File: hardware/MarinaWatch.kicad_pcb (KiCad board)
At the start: 2 copper layers, 70 x 101 mm, 59 parts, among them J201 USB_C_Receptacle_USB2.0_16P, J401 Screw_Terminal_01x04, J801 Screw_Terminal_01x02, J802 Screw_Terminal_01x03, U101 ESP32-S3-MINI-1, U301 LMV321, U302 LMV321, U303 LMV321, U501 BQ24210, U601 BQ24210, U701 TPS63070

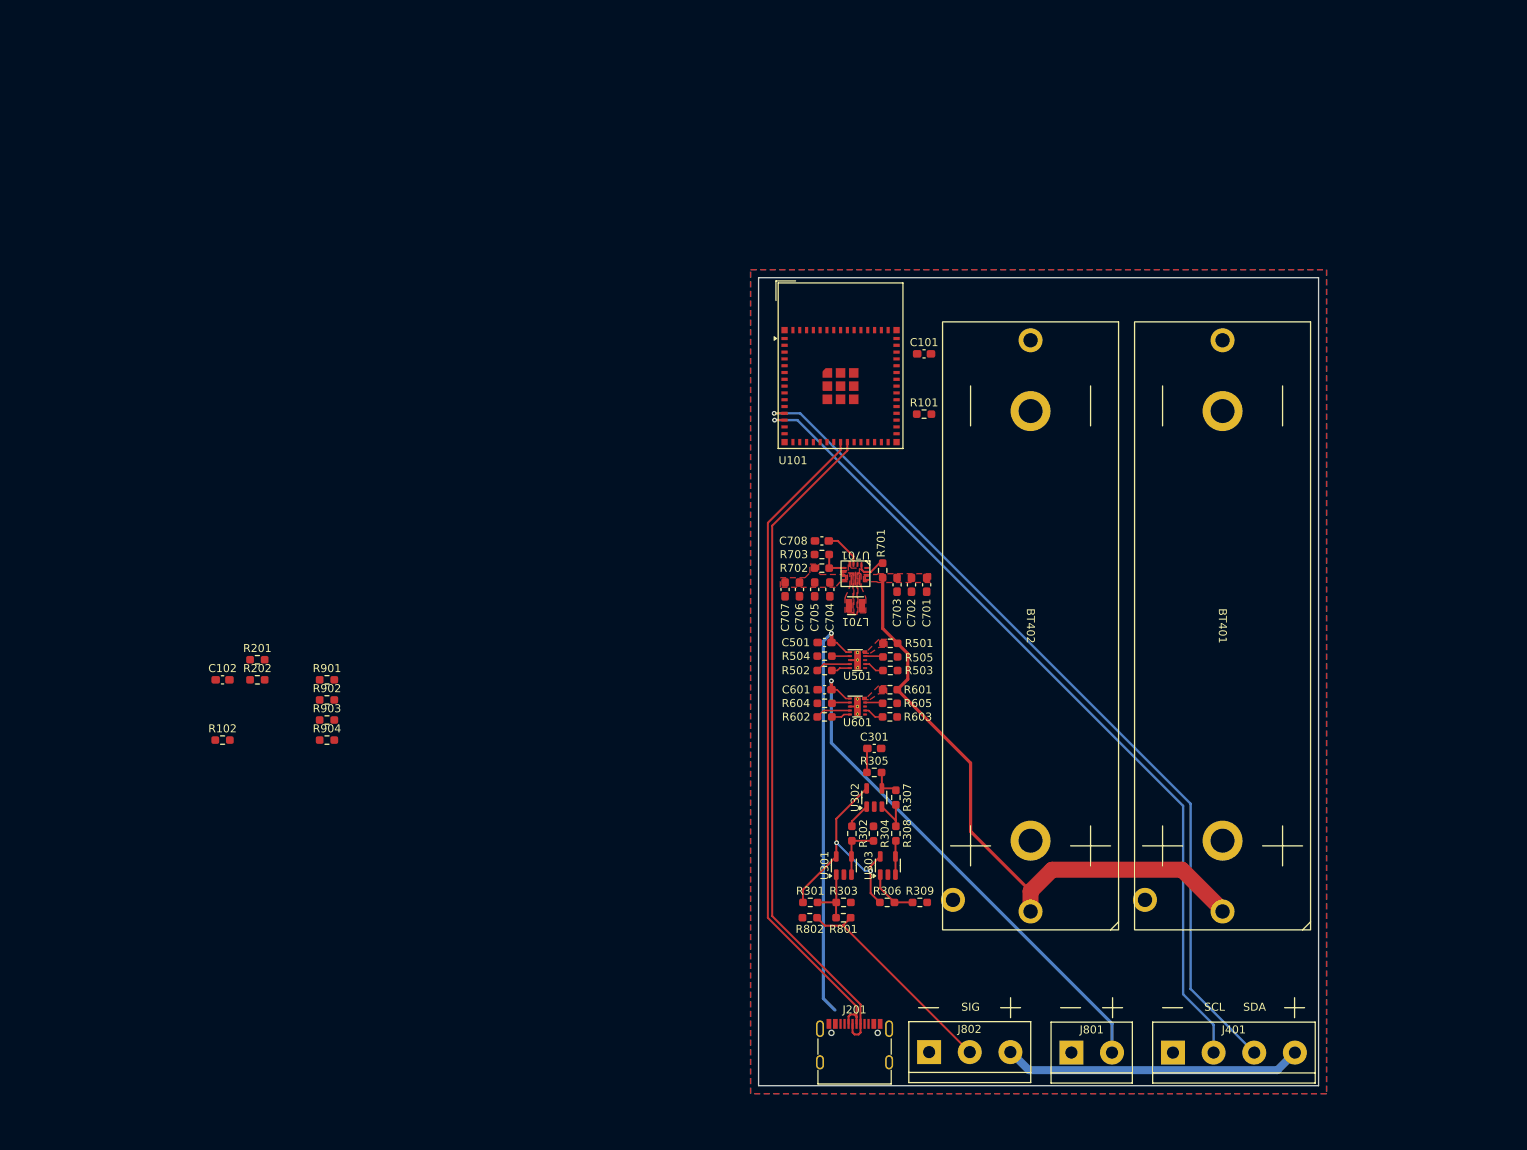
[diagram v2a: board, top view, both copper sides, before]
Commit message: Layout almost finished (missing NTCs and Buttons)
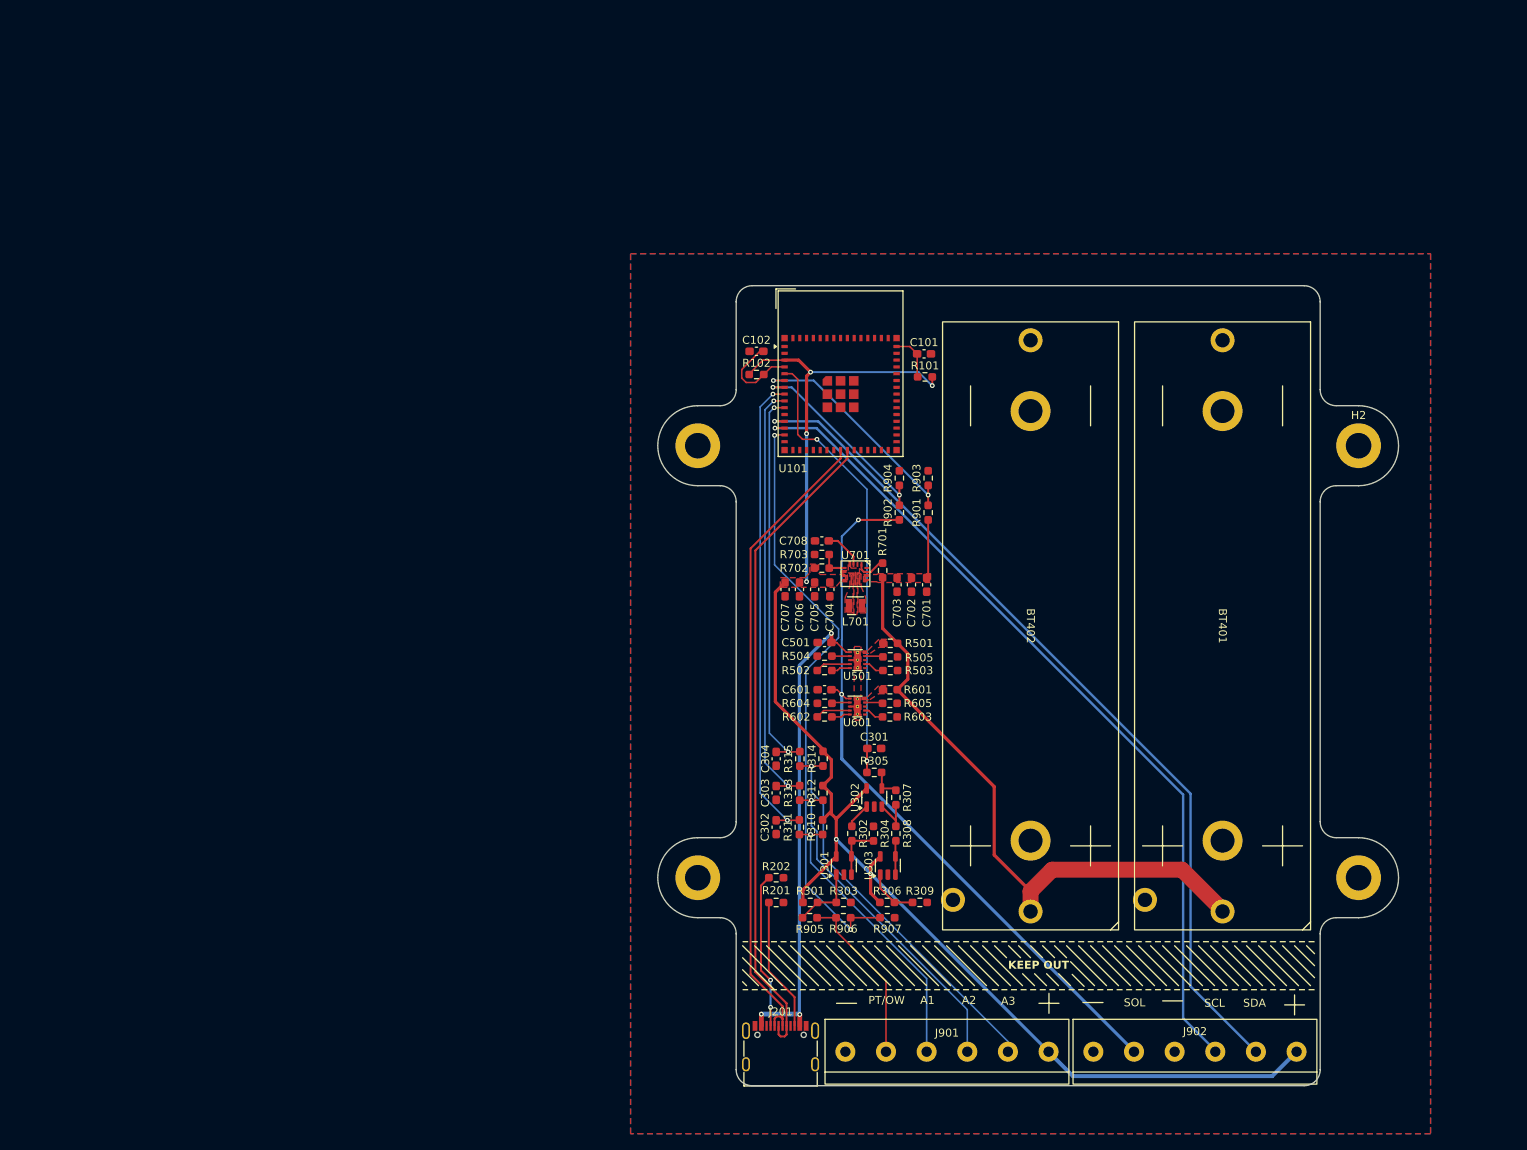
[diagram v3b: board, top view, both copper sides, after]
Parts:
- removed J401: Screw_Terminal_01x04, TerminalBlock:TerminalBlock_bornier-4_P5.08mm
- removed J801: Screw_Terminal_01x02, TerminalBlock:TerminalBlock_bornier-2_P5.08mm
- removed J802: Screw_Terminal_01x03, TerminalBlock:TerminalBlock_bornier-3_P5.08mm
- removed R801, R802: 100R, Resistor_SMD:R_0603_1608Metric_Pad0.98x0.95mm_HandSolder
- added C302: 22u, Capacitor_SMD:C_0603_1608Metric_Pad1.08x0.95mm_HandSolder, F.Cu at (128.2, 121.7)
- added C303: 22u, Capacitor_SMD:C_0603_1608Metric_Pad1.08x0.95mm_HandSolder, F.Cu at (128.2, 117.4)
- added C304: 22u, Capacitor_SMD:C_0603_1608Metric_Pad1.08x0.95mm_HandSolder, F.Cu at (128.2, 113.1)
- added H1: MountingHole_Pad, MountingHole:MountingHole_3.2mm_M3_DIN965_Pad, F.Cu at (118.4, 74.0)
- added H2: MountingHole_Pad, MountingHole:MountingHole_3.2mm_M3_DIN965_Pad, F.Cu at (201.0, 74.0)
- added H3: MountingHole_Pad, MountingHole:MountingHole_3.2mm_M3_DIN965_Pad, F.Cu at (118.4, 128.0)
- added H4: MountingHole_Pad, MountingHole:MountingHole_3.2mm_M3_DIN965_Pad, F.Cu at (201.0, 128.0)
- added J901: Screw_Terminal_01x06, AlfredLib:THT_SCREW_01x06_P5.08mm, F.Cu at (149.6, 149.8)
- added J902: Screw_Terminal_01x06, AlfredLib:THT_SCREW_01x06_P5.08mm, F.Cu at (180.6, 149.8)
- added R310: 10k, Resistor_SMD:R_0603_1608Metric_Pad0.98x0.95mm_HandSolder, F.Cu at (134.0, 121.7)
- added R311: 100R, Resistor_SMD:R_0603_1608Metric_Pad0.98x0.95mm_HandSolder, F.Cu at (131.1, 121.7)
- added R312: 10k, Resistor_SMD:R_0603_1608Metric_Pad0.98x0.95mm_HandSolder, F.Cu at (134.0, 117.4)
- added R313: 100R, Resistor_SMD:R_0603_1608Metric_Pad0.98x0.95mm_HandSolder, F.Cu at (131.1, 117.4)
- added R314: 10k, Resistor_SMD:R_0603_1608Metric_Pad0.98x0.95mm_HandSolder, F.Cu at (134.1, 113.1)
- added R315: 100R, Resistor_SMD:R_0603_1608Metric_Pad0.98x0.95mm_HandSolder, F.Cu at (131.2, 113.1)
- added R905: 0R, Resistor_SMD:R_0603_1608Metric_Pad0.98x0.95mm_HandSolder, F.Cu at (132.4, 133.0)
- added R906: 0R, Resistor_SMD:R_0603_1608Metric_Pad0.98x0.95mm_HandSolder, F.Cu at (136.6, 133.0)
- added R907: 10k, Resistor_SMD:R_0603_1608Metric_Pad0.98x0.95mm_HandSolder, F.Cu at (142.1, 133.0)
- moved R903 81.0 mm to (147.2, 78.0), turned to 90 degrees
- moved R102 80.9 mm to (125.7, 65.1)
- moved R904 78.7 mm to (143.6, 78.0), turned to 90 degrees
- moved C102 78.4 mm to (125.7, 62.2), turned to 180 degrees
- moved R901 78.0 mm to (147.2, 82.4), turned to 90 degrees
- moved R902 75.3 mm to (143.6, 82.4), turned to 90 degrees
- moved R201 71.6 mm to (128.2, 131.1)
- moved R202 69.4 mm to (128.2, 128.0)
- moved J201 9.25 mm to (128.8, 150.2)
- moved R101 4.65 mm to (146.8, 65.4), turned to 180 degrees
- moved U101 1.00 mm to (136.2, 65.0)
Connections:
- net Net-(J201-CC1) renamed /CC1
- net Net-(J201-CC2) renamed /CC2
- U101 pad 10: unconnected-(U101-IO6-Pad10) -> /A3
- U101 pad 8: unconnected-(U101-IO4-Pad8) -> /A1
- U101 pad 9: unconnected-(U101-IO5-Pad9) -> /A2
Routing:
- net +3V3: track 67.4 -> 183.5 mm, vias 2 -> 6
- net /ONE_WIRE: track 0.00 -> 75.6 mm, vias 0 -> 2
- net /A1: track 0.00 -> 59.7 mm, vias 0 -> 2
- net /TEMP_SENS: track 3.02 -> 57.3 mm, vias 0 -> 2
- net /A2: track 0.00 -> 54.1 mm, vias 0 -> 2
- net /ANALOG_3: track 0.00 -> 48.8 mm, vias 0 -> 1
- net /A3: track 0.00 -> 48.5 mm, vias 0 -> 2
- net /ANALOG_2: track 0.00 -> 42.4 mm, vias 0 -> 1
- net /ANALOG_1: track 0.00 -> 36.1 mm, vias 0 -> 1
- net /BAT_SENSE: track 0.00 -> 29.2 mm, vias 0 -> 2
- net SOLAR: track 64.9 -> 90.4 mm, vias 1 -> 2
- net /SOLAR_SENSE: track 0.00 -> 25.4 mm, vias 0 -> 2
- net /CC1: track 0.00 -> 19.4 mm, vias 0 -> 2
- net /CC2: track 0.00 -> 16.8 mm
- net /BOOT: track 0.00 -> 11.2 mm
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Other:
- board size 70 x 101 mm -> 92.6 x 100 mm
- board text added: "A1"
- board text added: "A2"
- board text added: "A3"
- board text added: "KEEP OUT"
- board text added: "PT/OW"
- board text added: "SOL"
- board text removed: "SIG"

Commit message: First draft of HW and moved scripts
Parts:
- added C103: 10u, Capacitor_SMD:C_0603_1608Metric_Pad1.08x0.95mm_HandSolder, F.Cu at (117.5, 99.4)
- added SW101: SW_Push, AlfredLib:BUTTON_SMD_3x4mm, F.Cu at (130.5, 32.7)
- added SW102: SW_Push, AlfredLib:BUTTON_SMD_3x4mm, F.Cu at (117.3, 110.9)
- added U304: ESP32-S3-WROOM-1, RF_Module:ESP32-S3-WROOM-1, F.Cu at (134.2, 67.1)
- R101, R102, R503, R603, R701: value 5k1 -> 10k
- R504: value 5k1 -> 511R
- R505: value 5k1 -> 6k8
- R605: value 5k1 -> 0R
- R904: value 7k5 -> 3k
- moved U101 115.0 mm to (41.5, 130.3)
- moved C101 42.8 mm to (130.9, 22.8)
- moved R101 42.8 mm to (131.1, 25.6)
- moved C102 41.5 mm to (116.3, 102.6), turned to 90 degrees
- moved R102 38.3 mm to (118.0, 102.6), turned to -90 degrees
- moved R902 5.23 mm to (144.5, 87.5)
- moved R904 5.23 mm to (144.5, 83.2)
- moved R901 5.05 mm to (147.4, 87.4)
- moved R903 5.05 mm to (147.4, 83.1)
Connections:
- U101 pad 10: /A3 -> unconnected-(U101-IO6-Pad10)
- U101 pad 12: /I2C_SDA -> unconnected-(U101-IO8-Pad12)
- U101 pad 13: /I2C_SCL -> unconnected-(U101-IO9-Pad13)
- U101 pad 14: /ONE_WIRE -> unconnected-(U101-IO10-Pad14)
- U101 pad 23: /D- -> unconnected-(U101-IO19-Pad23)
- U101 pad 24: /D+ -> unconnected-(U101-IO20-Pad24)
- U101 pad 4: /BOOT -> unconnected-(U101-IO0-Pad4)
- U101 pad 45: /RESET -> unconnected-(U101-EN-Pad45)
- U101 pad 5: /TEMP_SENS -> unconnected-(U101-IO1-Pad5)
- U101 pad 6: /BAT_SENSE -> unconnected-(U101-IO2-Pad6)
- U101 pad 7: /SOLAR_SENSE -> unconnected-(U101-IO3-Pad7)
- U101 pad 8: /A1 -> unconnected-(U101-IO4-Pad8)
- U101 pad 9: /A2 -> unconnected-(U101-IO5-Pad9)
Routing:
- net /I2C_SDA: track 108.2 -> 35.6 mm, vias 1 -> 0
- net /I2C_SCL: track 105.0 -> 33.8 mm, vias 1 -> 0
- net +3V3: track 183.5 -> 154.9 mm, vias 6 -> 4
- net /SOLAR_SENSE: track 25.4 -> 2.49 mm, vias 2 -> 0
- net /D+: track 81.7 -> 73.8 mm
- net +BATT: track 87.1 -> 80.1 mm
- net /D-: track 80.4 -> 74.6 mm
- net /RESET: track 5.86 -> 10.9 mm
- net /BAT_SENSE: track 29.2 -> 24.6 mm, vias 2 -> 0
- net /A1: track 59.7 -> 56.0 mm, vias 2 -> 1
- net /A2: track 54.1 -> 51.3 mm, vias 2 -> 1
- net /BOOT: track 11.2 -> 8.61 mm
- net SOLAR: track 90.4 -> 88.7 mm
- net /A3: track 48.5 -> 47.2 mm
- net /ONE_WIRE: track 75.6 -> 74.4 mm, vias 2 -> 1
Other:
- board text added: "BOOT"
- board text added: "RST"

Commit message: Added NTCs
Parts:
- added TH501: 4k7 @ 25C, Resistor_SMD:R_0603_1608Metric_Pad0.98x0.95mm_HandSolder, F.Cu at (116.3, 89.7)
- added TH601: 4k7 @ 25C, Resistor_SMD:R_0603_1608Metric_Pad0.98x0.95mm_HandSolder, F.Cu at (116.3, 92.2)
- R502, R602: value 5k1 -> 9k8
- R604: value 5k1 -> 3k9

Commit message: Recond draft of HW
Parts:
- removed U101: ESP32-S3-MINI-1, RF_Module:ESP32-S2-MINI-1
- added R316: 0R, Resistor_SMD:R_0603_1608Metric_Pad0.98x0.95mm_HandSolder, F.Cu at (126.7, 101.0)
- BT402: moved to B.Cu
- moved C101 68.0 mm to (126.8, 90.7)
- moved TH601 64.4 mm to (179.5, 104.2), turned to 180 degrees
- moved TH501 63.7 mm to (179.6, 96.6), turned to 180 degrees
- moved R101 62.4 mm to (126.8, 87.8)
- moved SW101 62.1 mm to (126.8, 94.8)
- moved C304 52.8 mm to (169.5, 80.3)
- moved R315 52.8 mm to (172.5, 80.3)
- moved R314 52.8 mm to (175.4, 80.3)
- moved C303 52.3 mm to (168.7, 84.3)
- moved R312 52.3 mm to (174.5, 84.3)
- moved R313 52.3 mm to (171.6, 84.3)
- moved C701 52.0 mm to (198.7, 85.0)
- moved C704 52.0 mm to (186.6, 85.6)
- moved C705 52.0 mm to (184.7, 85.6)
- moved C708 52.0 mm to (185.6, 79.5)
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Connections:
- U304 pad 4: /A1 -> /A3
- U304 pad 6: /A3 -> /A1
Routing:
- net +3V3: track 154.9 -> 217.2 mm, vias 4 -> 8
- net VBUS: track 61.0 -> 116.2 mm, vias 3 -> 2
- net /I2C_SDA: track 35.6 -> 81.4 mm, vias 0 -> 1
- net /ONE_WIRE: track 74.4 -> 30.2 mm, vias 1 -> 2
- net /TEMP_SENS: track 57.6 -> 14.3 mm, vias 2 -> 0
- net /ANALOG_1: track 36.1 -> 74.5 mm, vias 1 -> 0
- net /I2C_SCL: track 33.8 -> 68.5 mm, vias 0 -> 1
- net /ANALOG_2: track 42.4 -> 77.1 mm, vias 1 -> 0
- net /ANALOG_3: track 48.8 -> 80.4 mm, vias 1 -> 0
- net /SIG: track 21.7 -> 52.2 mm
- net /BOOT: track 8.61 -> 38.5 mm, vias 0 -> 2
- net /D-: track 74.6 -> 51.1 mm
- net /D+: track 73.8 -> 50.9 mm
- net /SOLAR_SENSE: track 2.49 -> 25.2 mm, vias 0 -> 2
- net /BAT_SENSE: track 24.6 -> 7.01 mm
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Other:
- board size 92.6 x 100 mm -> 97.1 x 78 mm
- board text added: "RESET"
- board text removed: "RST"

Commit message: Calculating values
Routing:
- net GND: vias 461 -> 451
